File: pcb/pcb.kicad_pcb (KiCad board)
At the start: 2 copper layers, 99.7 x 99.7 mm, 61 parts, among them CN1 Battery, CN10 Pump_On, CN11 Pump_Drain, CN2 Bat_Sense, CN3 VBUS, CN4 3.3V, CN5 VIMM, CN6 ~{Soil_On}, CN7 Soil_Drain, CN8 Soil_Out, CN9 Water_Out, Q1 2N7002, Q2 AO3401A, Q3 AO3400A, U1 USB-C 6PIN, U2 TPS63802DLAT, U3 BQ24075RGTR, U4 TUSB320LIRWBR, U5 ESP-32S DevBoard, U6 Water_Sensor, U7 Pump

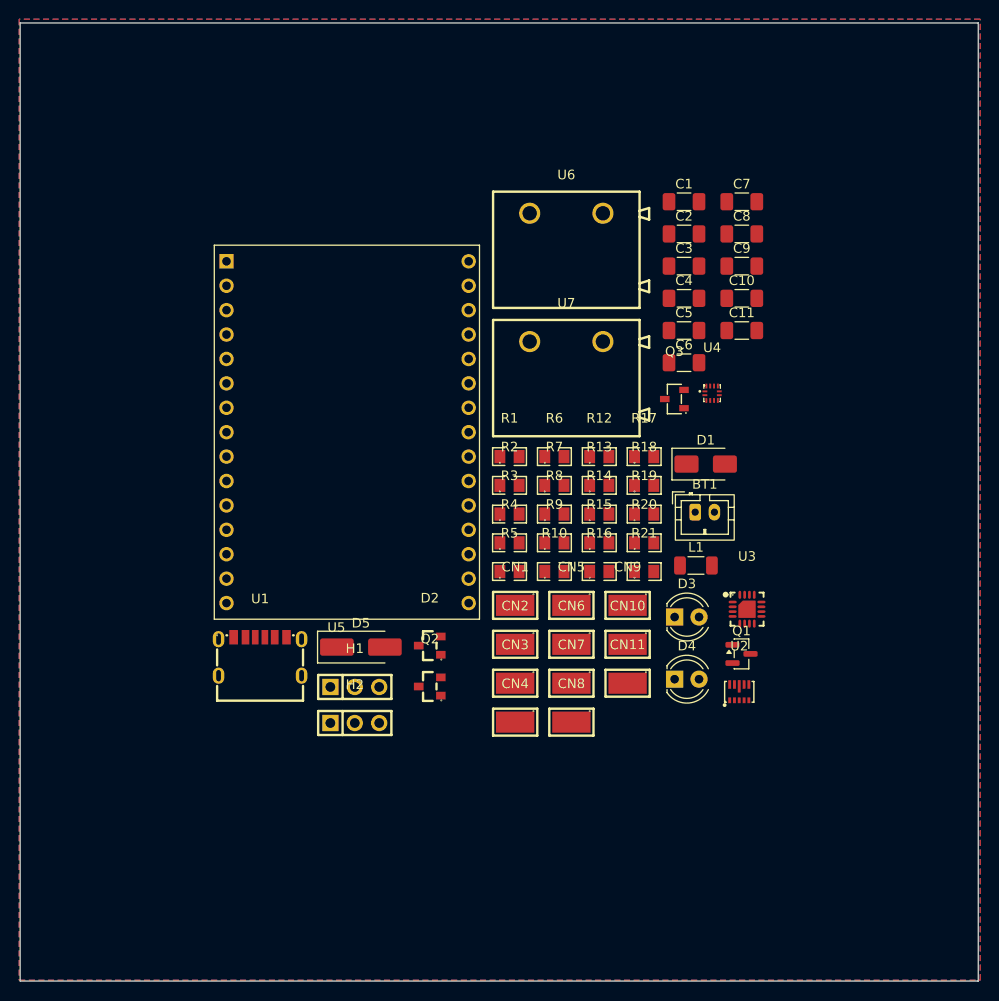
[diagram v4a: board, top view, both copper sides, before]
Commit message: Replaced even more components with 0805 equivalents
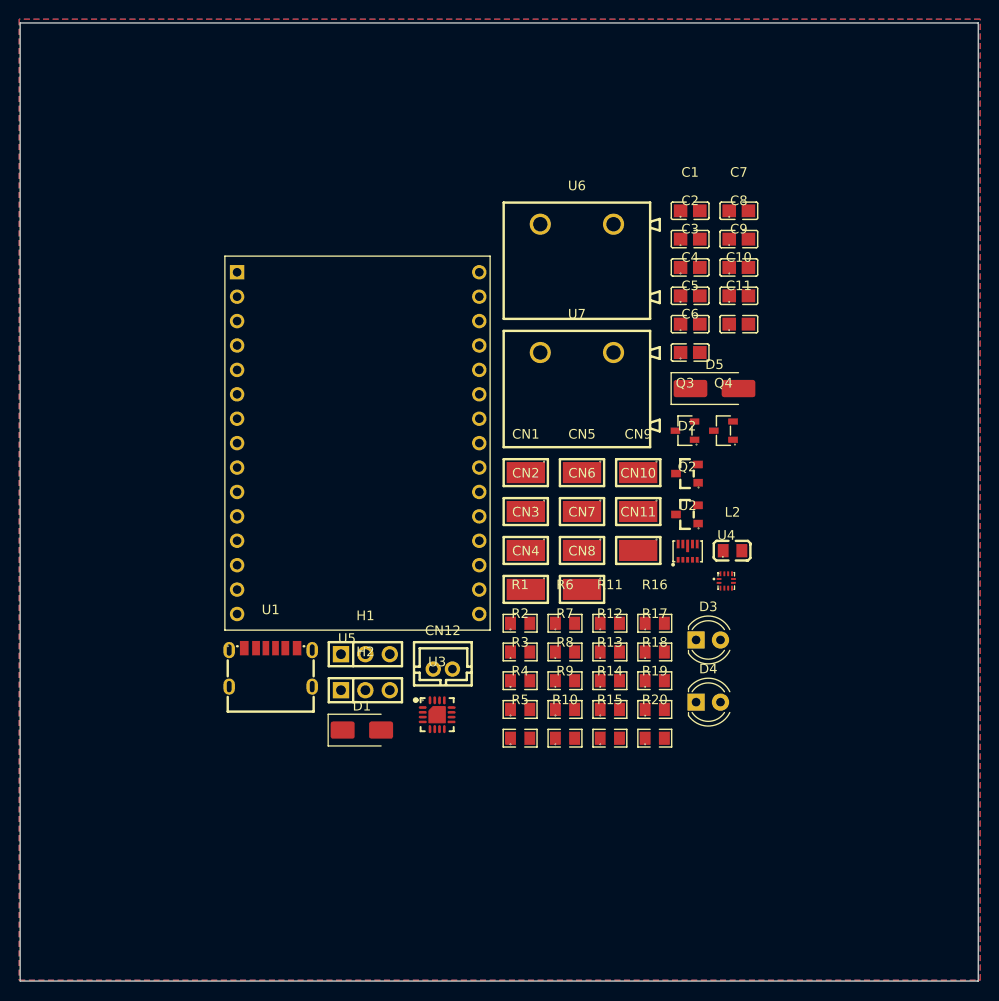
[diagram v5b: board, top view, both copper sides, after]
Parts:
- removed BT1: Battery_Cell, Connector_JST:JST_PH_B2B-PH-K_1x02_P2.00mm_Vertical
- removed L1: 0.47uH, Inductor_SMD:L_1206_3216Metric_Pad1.22x1.90mm_HandSolder
- removed Q1: 2N7002, Package_TO_SOT_SMD:SOT-23
- removed R21: 900k, EasyEDA:R0805
- added CN12: Battery_Cell, EasyEDA:CONN-TH_B2B-PH-K-S, F.Cu at (144.3, 120.4)
- added L2: 470nH, EasyEDA:L0805, F.Cu at (174.5, 108.1)
- added Q4: 2N7002, EasyEDA:SOT-23-3_L2.9-W1.3-P1.90-LS2.4-BR, F.Cu at (173.5, 95.6)
- added R11: 47k, EasyEDA:R0805, F.Cu at (161.7, 115.6)
- C1, C10, C11, C2, C3, C4, C5, C6, C7, C8, C9: footprint Capacitor_SMD:C_1206_3216Metric_Pad1.33x1.80mm_HandSolder -> EasyEDA:C0805
- R9: value 47k -> 900k
- moved D5 45.6 mm to (172.6, 91.2)
- moved D1 45.2 mm to (135.9, 126.8)
- moved U3 34.1 mm to (143.7, 125.2)
- moved D2 32.2 mm to (169.7, 100.1)
- moved Q2 32.2 mm to (169.7, 104.3)
- moved R12 20.4 mm to (161.7, 118.6)
- moved R13 20.4 mm to (161.7, 121.6)
- moved R15 20.4 mm to (161.7, 127.6)
- moved R17 20.4 mm to (166.4, 118.6)
- moved R18 20.4 mm to (166.4, 121.6)
- moved R20 20.4 mm to (166.4, 127.6)
- moved R14 20.4 mm to (161.7, 124.6)
- moved R19 20.4 mm to (166.4, 124.6)
- moved U4 19.6 mm to (173.8, 111.2)
- moved R2 17.4 mm to (152.4, 118.6)
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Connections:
- C1 pad 1: BAT_SENSE -> GND
- C1 pad 2: GND -> BAT_SENSE
- C5 pad 1: GND -> VIMM
- C5 pad 2: VIMM -> GND
- C8 pad 1: GND -> +3.3V
- C8 pad 2: +3.3V -> GND
- C9 pad 1: SOIL_OUT -> GND
- C9 pad 2: GND -> SOIL_OUT
- R10 pad 2: EN1 -> EN2
- R9 pad 1: +3.3V -> VBUS
- R9 pad 2: EN2 -> Net-(U4-VBUS_DET)

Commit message: Renamed the custom library from pcb to custom
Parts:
- U5: footprint pcb:ESP-32S_USB-C_CH340_DevBoard -> custom:ESP-32S_USB-C_CH340_DevBoard
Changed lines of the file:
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@@
 		)
 	)
-	(footprint "pcb:ESP-32S_USB-C_CH340_DevBoard"
+	(footprint "custom:ESP-32S_USB-C_CH340_DevBoard"
 		(layer "F.Cu")
 		(at 122.925 79.125)

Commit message: Fixed some ERC issues
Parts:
- removed H1: Power_Select, EasyEDA:HDR-TH_3P-P2.54-V-M_PZ254V-11-03P
- removed L2: 470nH, EasyEDA:L0805
- removed Q4: 2N7002, EasyEDA:SOT-23-3_L2.9-W1.3-P1.90-LS2.4-BR
- added L1: 470nH, EasyEDA:L0805, F.Cu at (172.5, 112.7)
- added Q1: 2N7002, EasyEDA:SOT-23-3_L2.9-W1.3-P1.90-LS2.4-BR, F.Cu at (170.8, 98.1)
- CN1: value Battery -> Battery_Cell; footprint EasyEDA:TESTPOINT-SMD_L3.8-W2.0_RH-5019 -> EasyEDA:CONN-TH_B2B-PH-K-S
- CN10: value Pump_On -> Water_Out
- CN11: value Pump_Drain -> Pump_On
- CN12: value Battery_Cell -> Pump_Drain; footprint EasyEDA:CONN-TH_B2B-PH-K-S -> EasyEDA:TESTPOINT-SMD_L3.8-W2.0_RH-5019
- CN2: value Bat_Sense -> Battery
- CN3: value VBUS -> Bat_Sense
- CN4: value 3.3V -> VBUS
- CN5: value VIMM -> 3.3V
- CN6: value ~{Soil_On} -> VIMM
- CN7: value Soil_Drain -> ~{Soil_On}
- CN8: value Soil_Out -> Soil_Drain
- CN9: value Water_Out -> Soil_Out
- moved D1 49.6 mm to (172.8, 93.7)
- moved D5 46.0 mm to (138.2, 121.8)
- moved U2 40.6 mm to (135.3, 129.6)
- moved U4 38.9 mm to (139.3, 129.3)
- moved U3 33.6 mm to (173.0, 108.6)
- moved D2 32.6 mm to (145.3, 121.6)
- moved Q2 32.6 mm to (145.3, 125.9)
- moved CN5 30.0 mm to (154.2, 129.6)
- moved CN9 30.0 mm to (160.1, 129.6)
- moved CN12 22.2 mm to (165.9, 125.5)
- moved CN1 21.0 mm to (173.6, 103.9)
- moved R1 13.8 mm to (153.6, 101.9)
- moved R10 13.8 mm to (158.3, 113.9)
- moved R11 13.8 mm to (163.0, 101.9)
- moved R12 13.8 mm to (163.0, 104.9)
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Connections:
- CN1 pad 1: Net-(C3-Pad1) -> GND
- CN10 pad 1: PUMP_ON -> WATER_OUT
- CN11 pad 1: Net-(D5-A) -> PUMP_ON
- CN12 pad 1: GND -> Net-(D5-A)
- CN2 pad 1: BAT_SENSE -> Net-(C3-Pad1)
- CN3 pad 1: VBUS -> BAT_SENSE
- CN4 pad 1: +3.3V -> VBUS
- CN5 pad 1: VIMM -> +3.3V
- CN6 pad 1: ~{SOIL_ON} -> VIMM
- CN7 pad 1: Net-(Q2-D) -> ~{SOIL_ON}
- CN8 pad 1: SOIL_OUT -> Net-(Q2-D)
- CN9 pad 1: WATER_OUT -> SOIL_OUT
- U5 pad 30: Net-(U5-3V3) -> +3.3V

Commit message: Component cleanup
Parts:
- removed D4: LED, LED_THT:LED_D4.0mm
- removed D5: D_Schottky, Diode_SMD:D_SMA_Handsoldering
- removed H2: Soil_Sensor, EasyEDA:HDR-TH_3P-P2.54-V-M_PZ254V-11-03P
- added H1: Soil_Sensor, EasyEDA:HDR-TH_3P-P2.54-V-M_PZ254V-11-03P, F.Cu at (136.5, 116.9)
- added LED1: RED 2V, EasyEDA:LED-TH_BD3.0-P2.54-FD, F.Cu at (170.5, 113.7)
- added LED2: GREEN 2V, EasyEDA:LED-TH_BD4.0-P2.54-FD, F.Cu at (172.8, 104.3)
- D1: footprint Diode_SMD:D_SMA -> EasyEDA:SMA_L4.3-W2.6-LS5.2-RD
- D3: value LED -> Schottky 40V; footprint LED_THT:LED_D4.0mm -> EasyEDA:SMA_L4.3-W2.6-LS5.2-RD
- L1: footprint EasyEDA:L0805 -> EasyEDA:IND-SMD_L2.0-W1.6-1
- moved D1 45.9 mm to (135.8, 120.7)
- moved U2 40.3 mm to (175.1, 123.1)
- moved U4 37.6 mm to (175.2, 117.9)
- moved D3 35.5 mm to (135.8, 124.8)
- moved L1 10.6 mm to (170.4, 123.1)
- moved U3 10.4 mm to (170.9, 118.9)
- moved Q1 9.11 mm to (169.8, 89.1)
- moved Q3 9.11 mm to (173.8, 89.1)
- moved D2 5.02 mm to (143.1, 117.1)
- moved Q2 5.02 mm to (143.1, 121.4)
- moved C1 4.61 mm to (170.3, 70.7)
- moved C10 4.61 mm to (175.4, 79.6)
- moved C11 4.61 mm to (175.4, 82.5)
- moved C2 4.61 mm to (170.3, 73.7)
- moved C3 4.61 mm to (170.3, 76.6)
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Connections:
- CN12 pad 1: Net-(D5-A) -> Net-(Q3-D)
- D3 pad 1: Net-(D3-K) -> +3.3V
- D3 pad 2: Net-(D3-A) -> Net-(Q3-D)
- Q3 pad 3: Net-(D5-A) -> Net-(Q3-D)
- R12 pad 1: Net-(D3-A) -> Net-(LED1-Pad1)
- U3 pad 9: Net-(D3-K) -> Net-(U3-#CHG)
- U7 pad 1: Net-(D5-A) -> Net-(Q3-D)
